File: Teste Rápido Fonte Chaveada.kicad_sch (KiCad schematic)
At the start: 15 parts, among them SW1 SW_DPST_x2

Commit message: Atualização da placa v0.1 (@JefersonMarcante)
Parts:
- added CN1: W4505-20PDRDTXR, Library:W4505-20PDRDTXR, symbol Connector_Generic:Conn_02x10_Top_Bottom
- D1: renamed from D2; footprint (none) -> Library:LED_1206_HandSolder
- D2: renamed from D6; footprint (none) -> Library:LED_1206_HandSolder
- D3: footprint (none) -> Library:LED_1206_HandSolder
- D4: renamed from D5; footprint (none) -> Library:LED_1206_HandSolder
- D5: renamed from D7; footprint (none) -> Library:LED_1206_HandSolder
- D6: renamed from D1; footprint (none) -> Library:LED_1206_HandSolder
- D7: renamed from D4; footprint (none) -> Library:LED_1206_HandSolder
- R1: renamed from R6; footprint (none) -> Library:RES_1206_HandSolder
- R2: footprint (none) -> Library:RES_1206_HandSolder
- R3: renamed from R5; footprint (none) -> Library:RES_1206_HandSolder
- R4: renamed from R3; footprint (none) -> Library:RES_1206_HandSolder
- R5: renamed from R1; footprint (none) -> Library:RES_1206_HandSolder
- R6: renamed from R7; footprint (none) -> Library:RES_1206_HandSolder
- R7: renamed from R4; footprint (none) -> Library:RES_1206_HandSolder
- SW1: footprint (none) -> Library:SW_Push_1P1T_NO_6x6mm_H9.5mm
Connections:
- net +12V: now also CN1.10 (Pin_10)
- net +3.3V: now also CN1.1 (Pin_1), CN1.11 (Pin_11), CN1.2 (Pin_2)
- net +5V: now also CN1.19 (Pin_19), CN1.20 (Pin_20), CN1.4 (Pin_4), CN1.6 (Pin_6)
- net -12V: now also CN1.12 (Pin_12)
- net -5V: now also CN1.18 (Pin_18)
- net GND: now also CN1.13 (Pin_13), CN1.15 (Pin_15), CN1.16 (Pin_16), CN1.17 (Pin_17), CN1.3 (Pin_3), CN1.5 (Pin_5), CN1.7 (Pin_7)
- net +P_G: now reaches R5.1
- net +P_G: now also CN1.8 (Pin_8)
- net +5V_SB: now reaches R6.1
- net +5V_SB: now also CN1.9 (Pin_9)
- net PS_ON: now reaches SW1.2 (B)
- net PS_ON: now also CN1.14 (Pin_14)

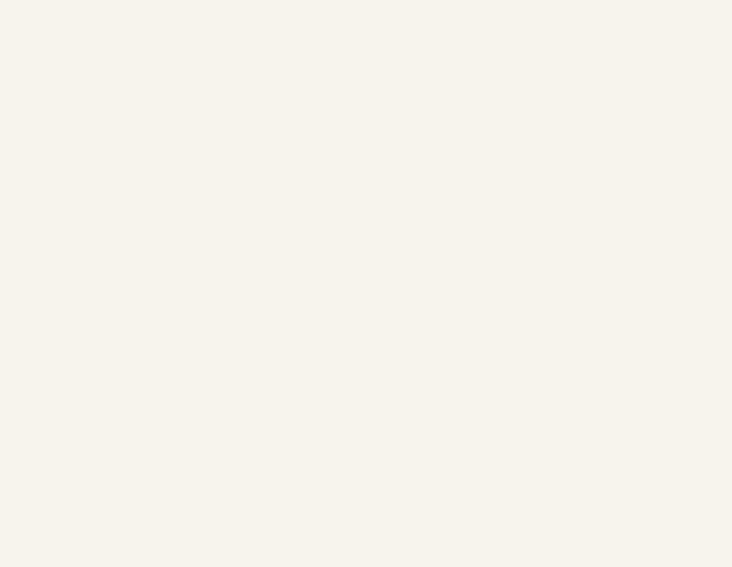
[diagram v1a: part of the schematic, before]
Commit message: Adicionado cargas de teste por Rail.
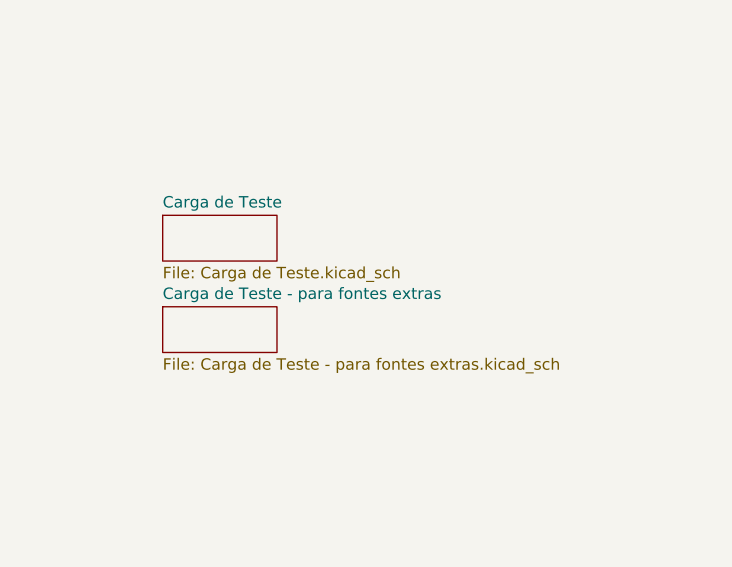
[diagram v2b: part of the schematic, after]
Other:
- added sheet Carga de Teste (Carga de Teste.kicad_sch)
- added sheet Carga de Teste - para fontes extras (Carga de Teste - para fontes extras.kicad_sch)
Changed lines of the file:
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@@
+		)
+	)
+	(sheet
+		(at 190.5 73.66)
+		(size 12.7 5.08)
+		(fields_autoplaced yes)
+		(stroke
+			(width 0.1524)
+			(type solid)
+		)
+		(fill
+			(color 0 0 0 0.0000)
+		)
+		(property "Sheetname" "Carga de Teste"
+			(at 190.5 72.9484 0)
+			(effects
+				(font
+					(size 1.27 1.27)
+				)
+				(justify left bottom)
+			)
+		)
+		(property "Sheetfile" "Carga de Teste.kicad_sch"
+			(at 190.5 79.3246 0)
+			(effects
+				(font
+					(size 1.27 1.27)
+				)
+				(justify left top)
+			)
+		)
+		(instances
+			(project "Teste Rápido Fonte Chaveada"
+				(path "/05a0489b-6f48-4980-a6d7-922522b33b13"
+					(page "2")
+				)
+			)
+		)
+	)
+	(sheet
+		(at 190.5 83.82)
+		(size 12.7 5.08)
+		(fields_autoplaced yes)
+		(stroke
+			(width 0.1524)
+			(type solid)
+		)
+		(fill
+			(color 0 0 0 0.0000)
+		)
+		(property "Sheetname" "Carga de Teste - para fontes extras"
+			(at 190.5 83.1084 0)
+			(effects
+				(font
+					(size 1.27 1.27)
+				)
+				(justify left bottom)
+			)
+		)
+		(property "Sheetfile" "Carga de Teste - para fontes extras.kicad_sch"
+			(at 190.5 89.4846 0)
+			(effects
+				(font
+					(size 1.27 1.27)
+				)
+				(justify left top)
+			)
+		)
+		(property "Campo2" ""
+			(at 190.5 83.82 0)
+			(effects
+				(font
+					(size 1.27 1.27)
+				)
+				(hide yes)
+			)
+		)
+		(instances
+			(project "Teste Rápido Fonte Chaveada"
+				(path "/05a0489b-6f48-4980-a6d7-922522b33b13"
+					(page "3")
+				)
+			)
 		)
 	)
